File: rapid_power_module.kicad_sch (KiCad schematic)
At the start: 26 parts, among them J1 Conn_02x04_Top_Bottom, J2 Molex MicroFit 2x2, J3 Conn_02x04_Top_Bottom, J4 Molex MicroFit 2x2, J5 Molex MicroFit 2x2, J6 Molex MicroFit 2x2, J7 Molex MicroFit 2x2

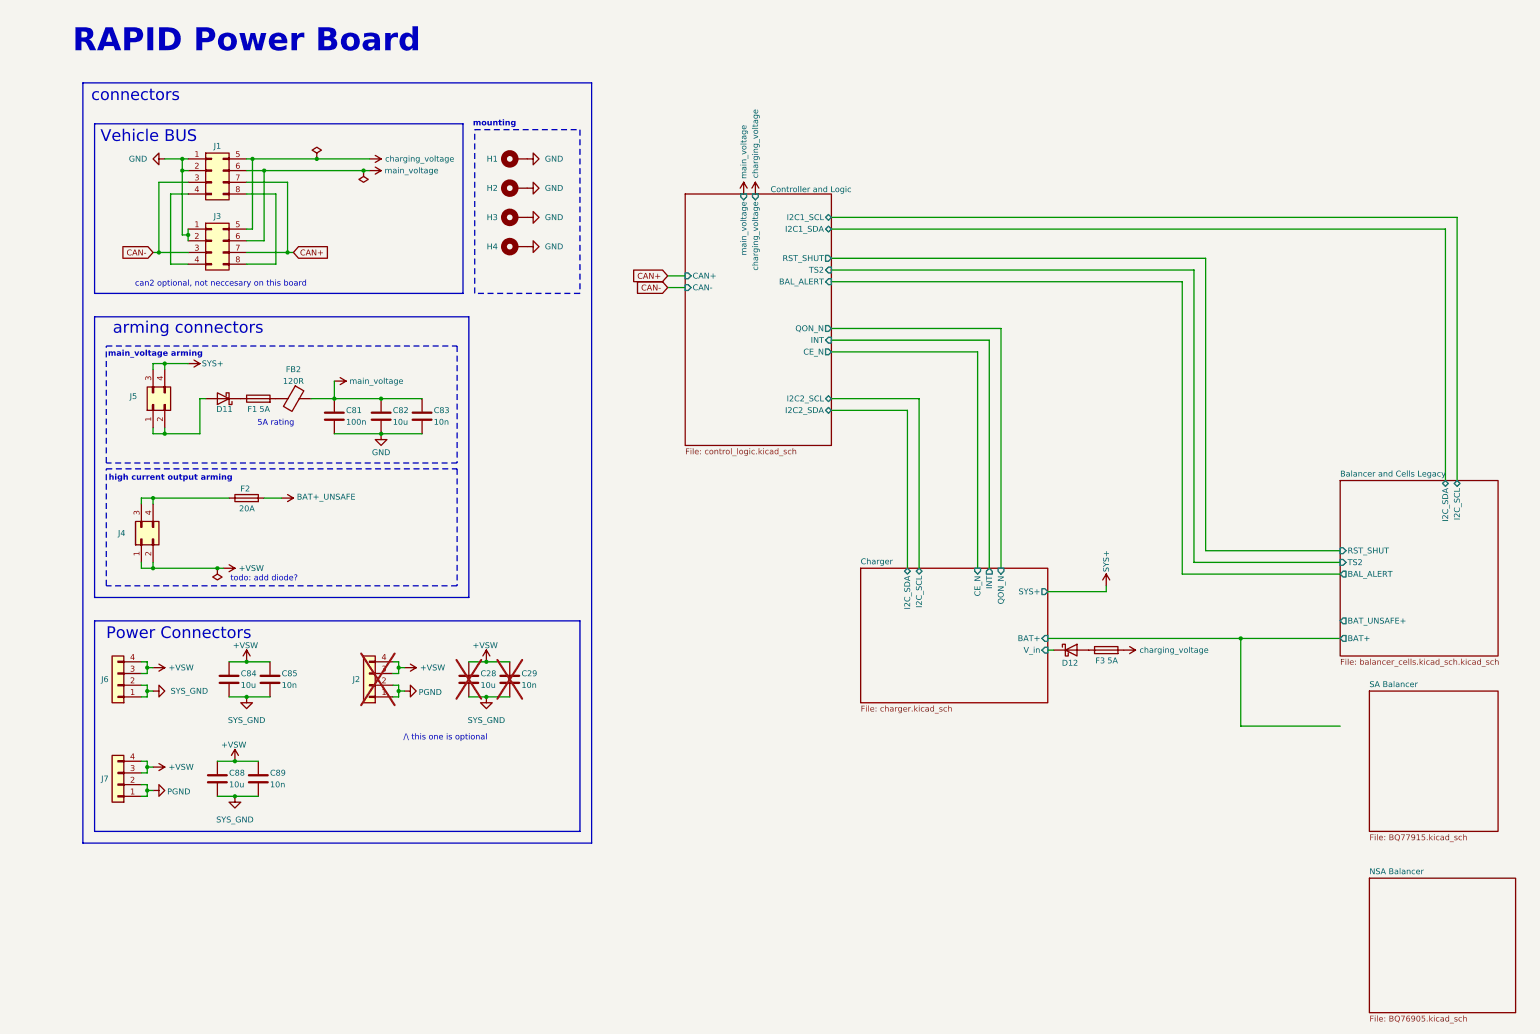
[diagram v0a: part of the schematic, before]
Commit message: Changed Balancer layout to support OVP, UVP and UVP-circumvention; added UVP-circumvention arming connector
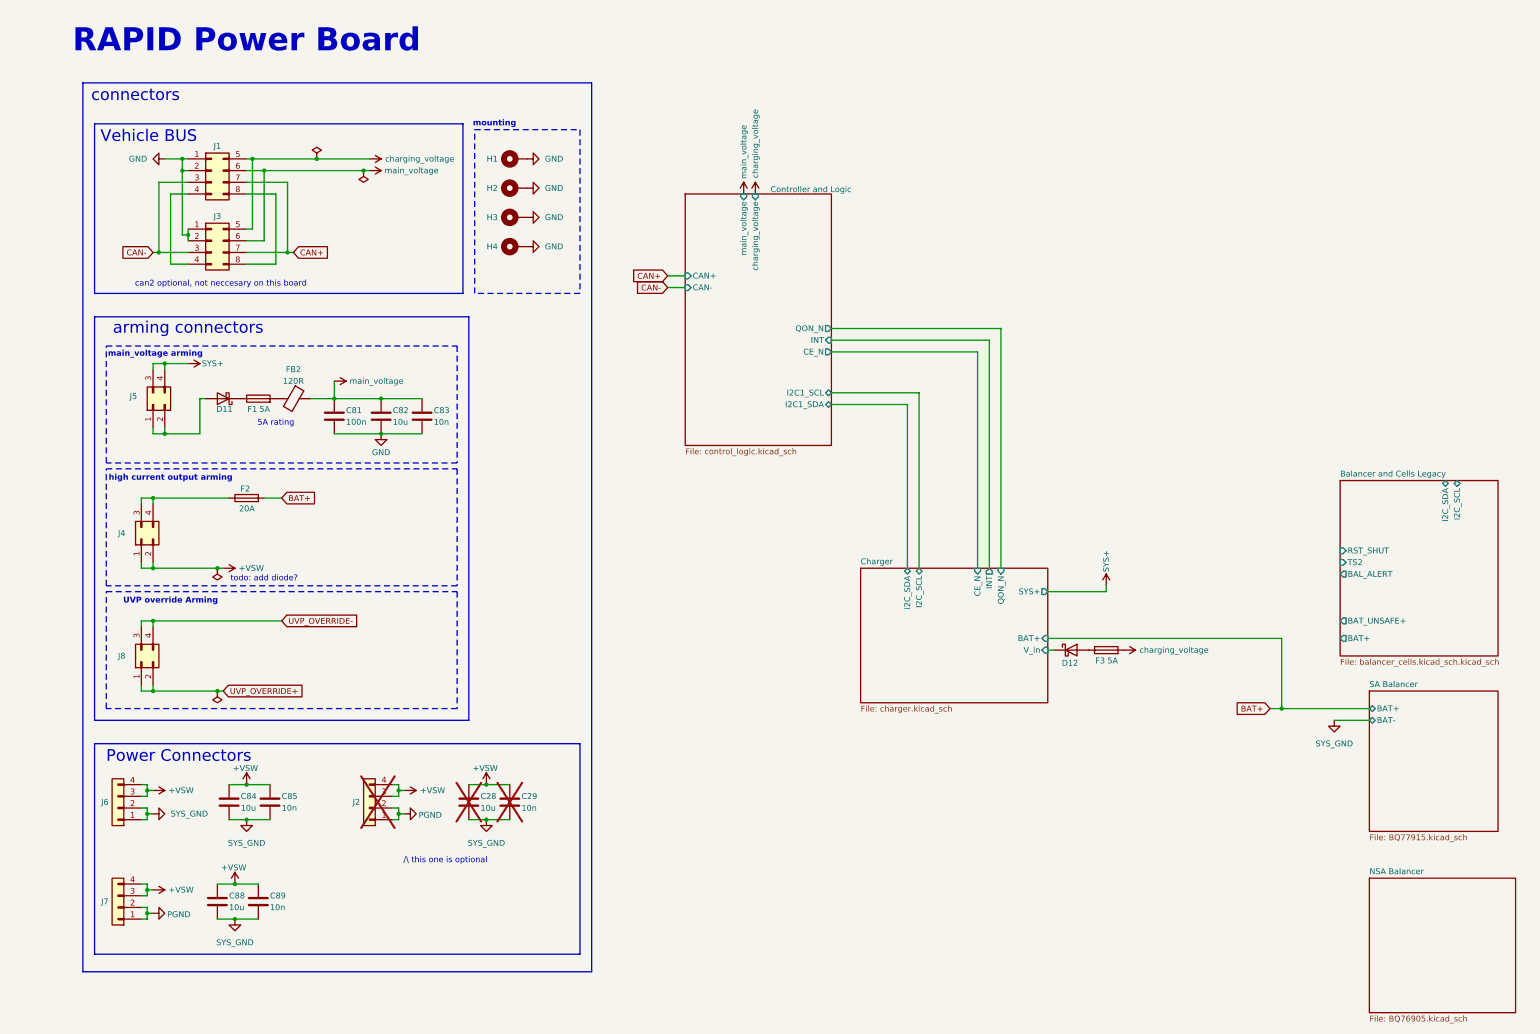
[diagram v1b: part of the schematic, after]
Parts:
- added J8: Molex MicroFit 2x2, Connector_Molex:Molex_Micro-Fit_3.0_43045-0400_2x02_P3.00mm_Horizontal, symbol Connector_Generic:Conn_02x02_Top_Bottom
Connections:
- net BAT+_UNSAFE renamed BAT+
- new net UVP_OVERRIDE+: J8.1 (Pin_1), J8.2 (Pin_2)
- new net UVP_OVERRIDE-: J8.3 (Pin_3), J8.4 (Pin_4)
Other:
- sheet Controller and Logic ports: added none; removed BAL_ALERT, I2C2_SCL, I2C2_SDA, RST_SHUT, TS2
- sheet SA Balancer ports: added BAT+, BAT-; removed none
- note added: "UVP override Arming"
- moved on the sheet: C28, C29, C84, C85, C88, C89, J2, J6, J7

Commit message: changed balancer layout according to new requirements (i.e. removed OVP/UVP, OTP/UTP, OCP/UCP); reduced arming connectors to only one
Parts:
- removed J4, J8: Molex MicroFit 2x2, Connector_Molex:Molex_Micro-Fit_3.0_43045-0400_2x02_P3.00mm_Horizontal, symbol Connector_Generic:Conn_02x02_Top_Bottom
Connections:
- net BAT+ is gone; now on an unnamed net: F2.2
- net +VSW: now also F2.1
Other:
- sheet SA Balancer renamed Balancer
- removed sheet Balancer and Cells Legacy
- removed sheet NSA Balancer
- note added: "Arming Connector"
- note removed: "Multiple Balancer Designs, only one should be kept."
- note removed: "UVP override Arming"
- note removed: "arming connectors"
- note removed: "high current output arming"
- note removed: "main_voltage arming"
- note removed: "todo: add diode?"
- moved on the sheet: C28, C29, C81, C82, C83, C84, C85, C88, C89, D11, F1, F2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

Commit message: added info text
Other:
- note added: "todo: - add diode for HCO? - does this setup make sense?"
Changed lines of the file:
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@@
+		)
+	)
+	(text "todo:\n- add diode for HCO?\n- does this setup make sense? "
+		(exclude_from_sim no)
+		(at 51.054 110.49 0)
+		(effects
+			(font
+				(size 1.27 1.27)
+			)
+			(justify left)
 		)
 	)

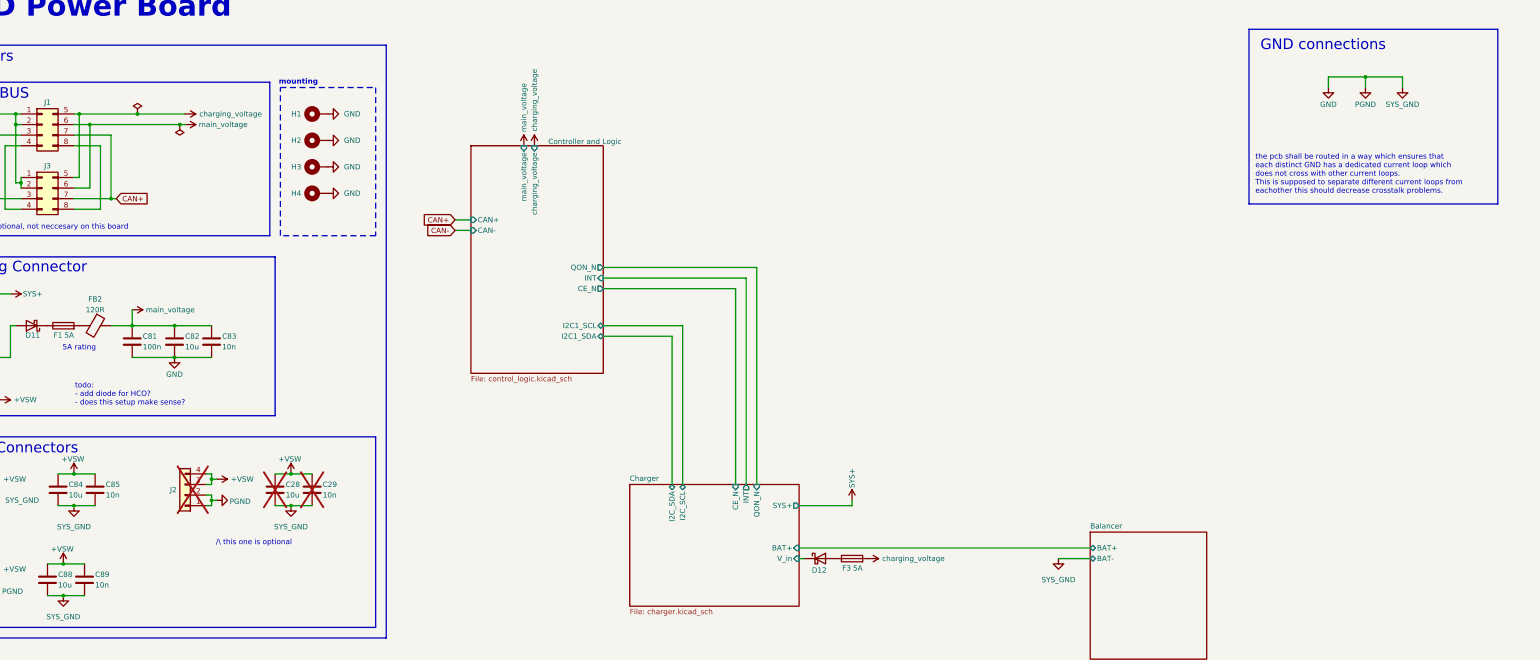
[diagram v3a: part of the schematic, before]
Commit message: finalized new balancer layout (removed R_SNS and implemented the resulting consequences); removed charger shipping mode
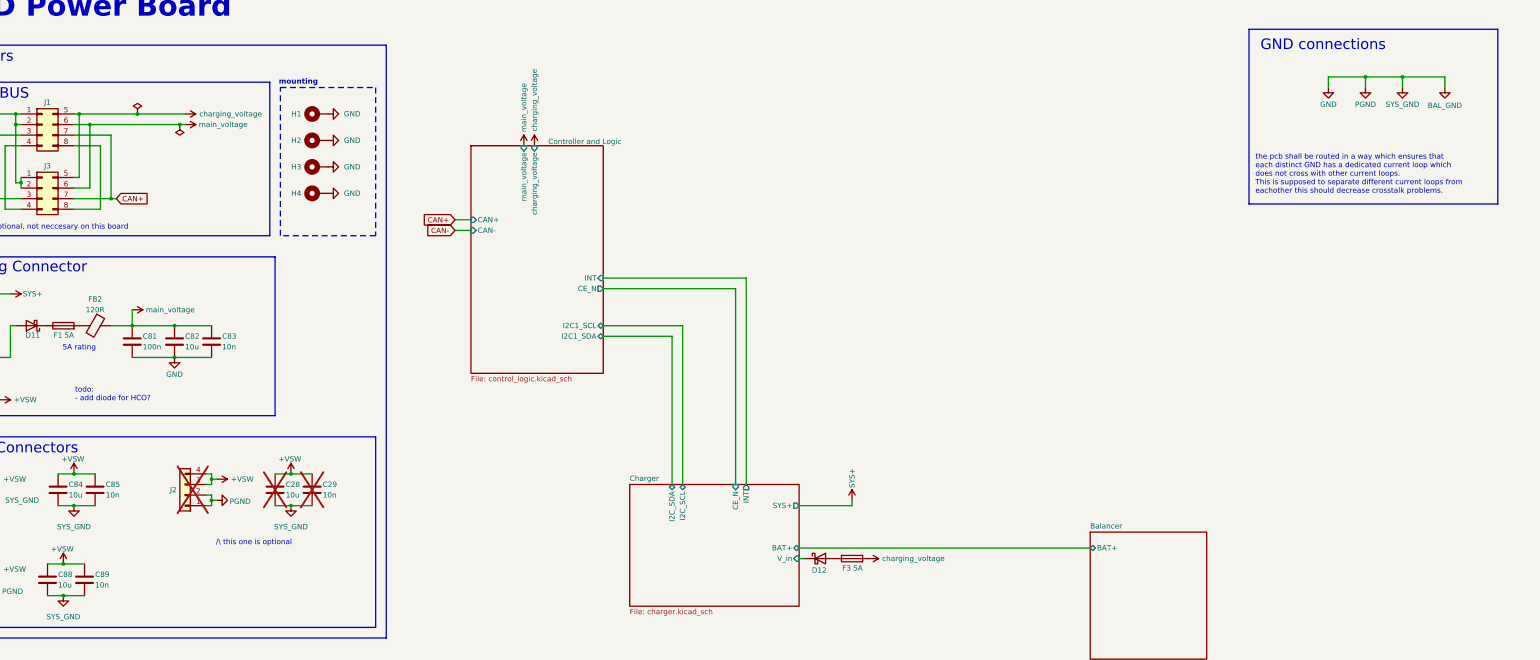
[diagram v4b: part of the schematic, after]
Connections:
- net GND renamed BAL_GND
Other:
- sheet Balancer ports: added none; removed BAT-
- sheet Charger ports: added none; removed QON_N
- sheet Controller and Logic ports: added none; removed QON_N
- note added: "todo: - add diode for HCO?"
- note removed: "todo: - add diode for HCO? - does this setup make sense?"
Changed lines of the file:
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@@
 		)
 	)
-	(text "todo:\n- add diode for HCO?\n- does this setup make sense? "
+	(text "todo:\n- add diode for HCO?"
 		(exclude_from_sim no)
 		(at 51.054 110.49 0)
@@
 	)
 	(junction
+		(at 369.57 34.29)
+		(diameter 0)
+		(color 0 0 0 0)
+	)
+	(junction
 		(at 36.83 45.72)
 		(diameter 0)
@@
 	(wire
 		(pts
-			(xy 214.63 80.01) (xy 214.63 132.08)
-		)
-		(stroke
-			(width 0)
-			(type default)
-		)
-	)
-	(wire
-		(pts
 			(xy 54.61 45.72) (xy 54.61 60.96)
 		)
@@
 	(wire
 		(pts
+			(xy 369.57 34.29) (xy 379.73 34.29)
+		)
+		(stroke
+			(width 0)
+			(type default)
+		)
+	)
+	(wire
+		(pts
 			(xy 83.82 135.89) (xy 85.09 135.89)
 		)
@@
 	(wire
 		(pts
-			(xy 287.02 149.86) (xy 294.64 149.86)
+			(xy 379.73 34.29) (xy 379.73 36.83)
 		)
 		(stroke
@@
 	(wire
 		(pts
-			(xy 177.8 80.01) (xy 214.63 80.01)
-		)
-		(stroke
-			(width 0)
-			(type default)
-		)
-	)
-	(wire
-		(pts
 			(xy 177.8 96.52) (xy 194.31 96.52)
 		)
@@
 	)
 	(symbol
-		(lib_id "power:GND")
-		(at 287.02 149.86 0)
-		(unit 1)
-		(exclude_from_sim no)
-		(in_bom yes)
-		(on_board yes)
-		(dnp no)
-		(fields_autoplaced yes)
-		(property "Reference" "#PWR035"
-			(at 287.02 156.21 0)
-			(effects
-				(font
-					(size 1.27 1.27)
-				)
-				(hide yes)
-			)
-		)
-		(property "Value" "SYS_GND"
-			(at 287.02 154.94 0)
-			(effects
-				(font
-					(size 1.27 1.27)
-				)
-			)
-		)
-		(property "Footprint" ""
-			(at 287.02 149.86 0)
-			(effects
-				(font
-					(size 1.27 1.27)
-				)
-				(hide yes)
-			)
-		)
-		(property "Datasheet" ""
-			(at 287.02 149.86 0)
-			(effects
-				(font
-					(size 1.27 1.27)
-				)
-				(hide yes)
-			)
-		)
-		(property "Description" ""
-			(at 287.02 149.86 0)
-			(effects
-				(font
-					(size 1.27 1.27)
-				)
-				(hide yes)
-			)
-		)
-		(pin "1"
-		)
-		(instances
-			(project "rapid_power_module"
-				(path "/afc8cbd3-9ea8-40a2-afae-ed6bd0fe7e6e"
-					(reference "#PWR035")
-					(unit 1)
-				)
-			)
-		)
-	)
-	(symbol
 		(lib_id "Mechanical:MountingHole_Pad")
 		(at 109.22 55.88 90)
@@
 	(symbol
 		(lib_id "power:GND")
+		(at 379.73 36.83 0)
+		(unit 1)
+		(exclude_from_sim no)
+		(in_bom yes)
+		(on_board yes)
+		(dnp no)
+		(property "Reference" "#PWR05"
+			(at 379.73 43.18 0)
+			(effects
+				(font
+					(size 1.27 1.27)
+				)
+				(hide yes)
+			)
+		)
+		(property "Value" "BAL_GND"
+			(at 379.73 41.148 0)
+			(effects
+				(font
+					(size 1.27 1.27)
+				)
+			)
+		)
+		(property "Footprint" ""
+			(at 379.73 36.83 0)
+			(effects
+				(font
+					(size 1.27 1.27)
+				)
+				(hide yes)
+			)
+		)
+		(property "Datasheet" ""
+			(at 379.73 36.83 0)
+			(effects
+				(font
+					(size 1.27 1.27)
+				)
+				(hide yes)
+			)
+		)
+		(property "Description" "Power symbol creates a global label with name \"GND\" , ground"
+			(at 379.73 36.83 0)
+			(effects
+				(font
+					(size 1.27 1.27)
+				)
+				(hide yes)
+			)
+		)
+		(pin "1"
+		)
+		(instances
+			(project "rapid_power_module"
+				(path "/afc8cbd3-9ea8-40a2-afae-ed6bd0fe7e6e"
+					(reference "#PWR05")
+					(unit 1)
+				)
+			)
+		)
+	)
+	(symbol
+		(lib_id "power:GND")
 		(at 48.26 158.75 0)
 		(unit 1)
@@
 			)
 		)
-		(pin "BAT+" input
-			(at 224.79 147.32 0)
-			(effects
-				(font
-					(size 1.27 1.27)
-				)
-				(justify right)
-			)
-		)
 		(pin "CE_N" input
 			(at 209.55 132.08 90)
@@
 			)
 		)
-		(pin "QON_N" input
-			(at 214.63 132.08 90)
-			(effects
-				(font
-					(size 1.27 1.27)
-				)
-				(justify right)
-			)
-		)
 		(pin "V_in" input
 			(at 224.79 149.86 0)
@@
 			)
 		)
+		(pin "BAT+" bidirectional
+			(at 224.79 147.32 0)
+			(effects
+				(font
+					(size 1.27 1.27)
+				)
+				(justify right)
+			)
+		)
 		(instances
 			(project "rapid_power_module"
@@
 			)
 		)
-		(pin "QON_N" output
-			(at 177.8 80.01 0)
-			(effects
-				(font
-					(size 1.27 1.27)
-				)
-				(justify right)
-			)
-		)
 		(pin "charging_voltage" input
 			(at 161.29 50.8 90)
@@
 			(effects
 				(font
-					(size 1.27 1.27)
-				)
-				(justify left)
-			)
-		)
-		(pin "BAT-" bidirectional
-			(at 294.64 149.86 180)
-			(effects
-				(font

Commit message: changed arming_pin2battery connection
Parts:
- added J4: Molex MicroFit 2x2, Connector_Molex:Molex_Micro-Fit_3.0_43045-0400_2x02_P3.00mm_Horizontal, symbol Connector_Generic:Conn_01x04
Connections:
- net BAL_GND: now also J4.3 (Pin_3), J4.4 (Pin_4)
- net SYS+ renamed V_BAT
- new net Charger/SYS+: J4.1 (Pin_1), J4.2 (Pin_2)
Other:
- note added: "\/ this one is optional"
- note removed: "5A rating"
- note removed: "todo: - add diode for HCO?"

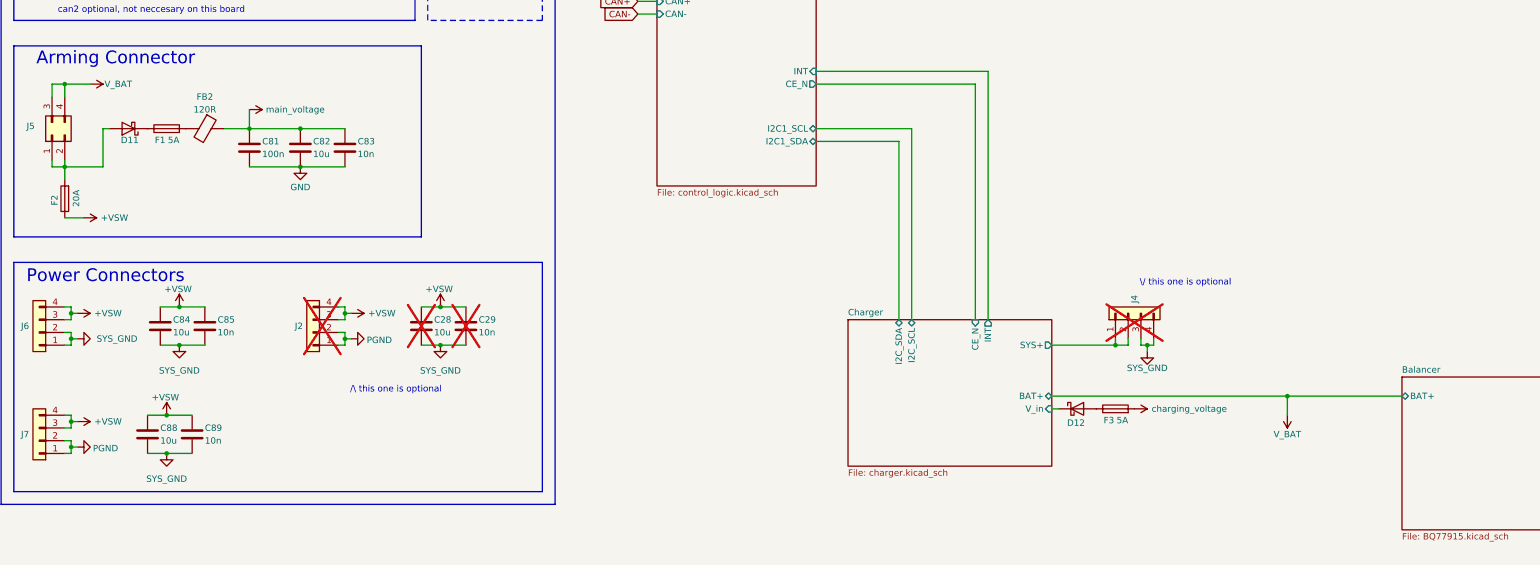
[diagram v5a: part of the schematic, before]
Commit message: implemented changes according to errors found in the schematic design review (wip)
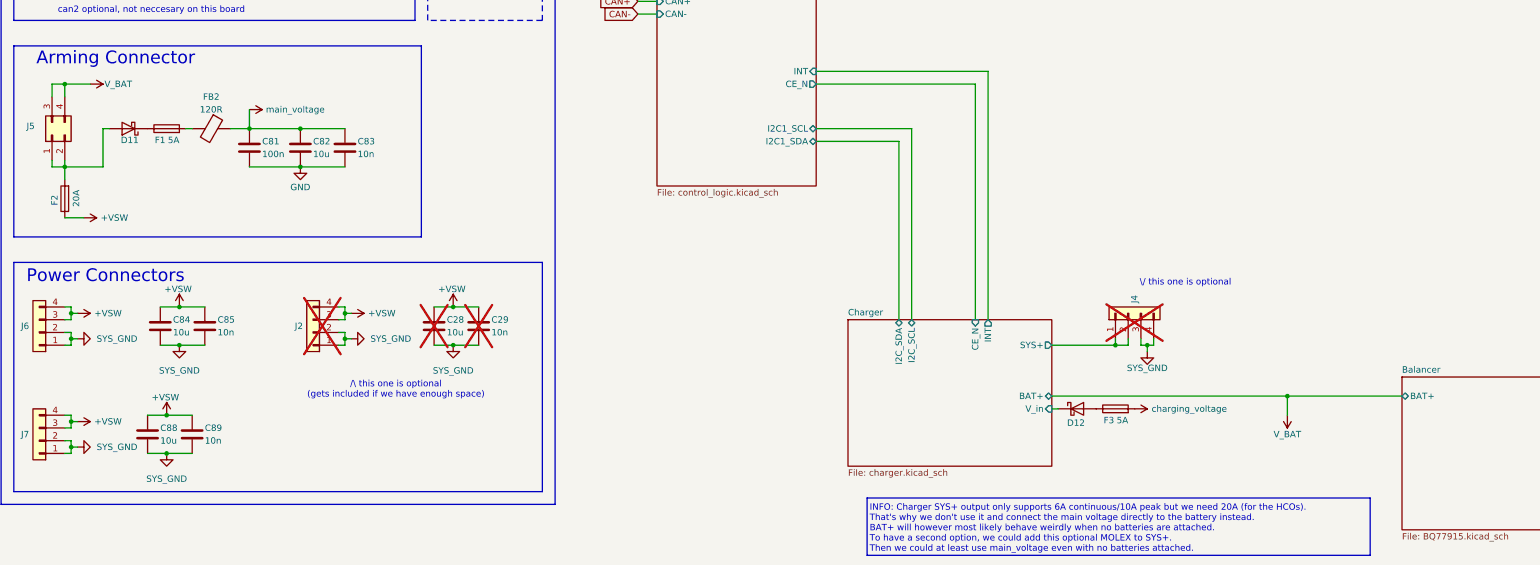
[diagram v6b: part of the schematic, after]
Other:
- note added: "/\ this one is optional (gets included if we have enough space)"
- note added: "INFO: Charger SYS+ output only supports 6A continuous/10A peak but we need 20A (for the HCOs). That's why we don't use it and connect the main voltage directly to the battery instead. BAT+ will however most likely behave weirdly when no batteries are attached. To have a second option, we could add this optional MOLEX to SYS+. Then we could at least use main_voltage even with no batteries attached."
- note removed: "/\ this one is optional"
- moved on the sheet: C28, C29, FB2
